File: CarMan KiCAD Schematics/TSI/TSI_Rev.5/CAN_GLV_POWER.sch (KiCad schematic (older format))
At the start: 35 parts, among them K2 G5LE-1-E, K3 SFS2-DC24V, K4 SFS2-DC24V, Q11 TN2130K1-G, U14 Bottom Left, U15 Top Left, U17 Top Right, U2 Bottom Right, U24 TLP293, U41 PDQ10-Q24-D5-D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

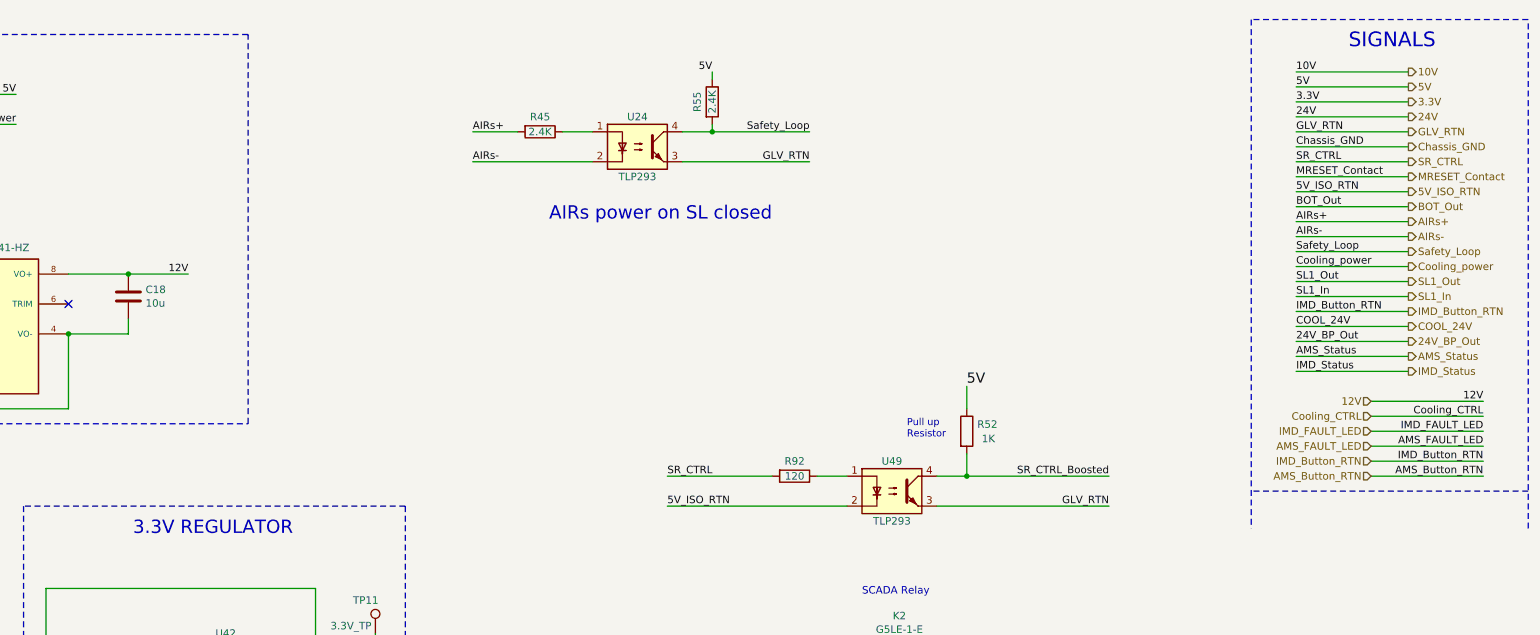
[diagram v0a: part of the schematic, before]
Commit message: Updated Signals and Trace Width
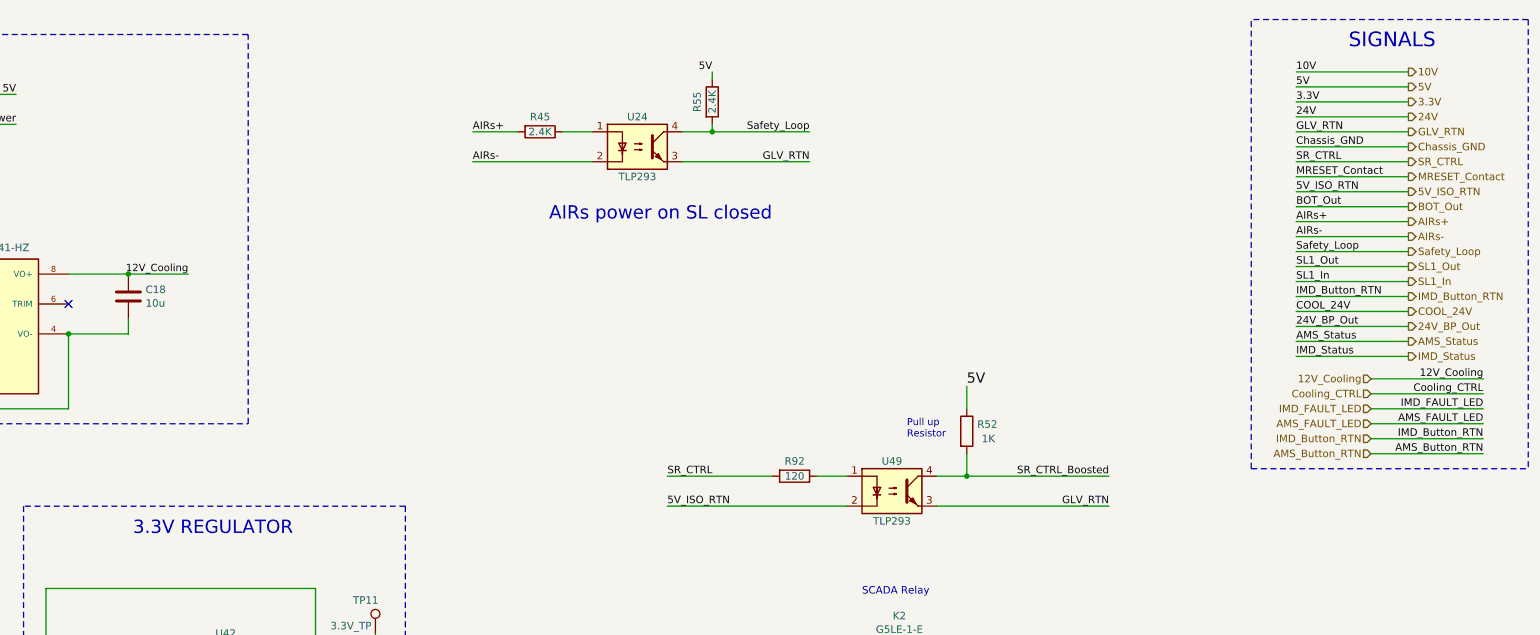
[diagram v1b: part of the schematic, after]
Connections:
- net labels added: 12V_Cooling
- net labels removed: 12V
- wire segments 175 -> 174
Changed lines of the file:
@@
 $Descr A3 16535 11693
 encoding utf-8
-Sheet 6 6
+Sheet 4 6
 Title ""
 Date ""
@@
 Zacky Bear Doesn't Like
 Text Label 7050 2250 2    49   ~ 0
-12V
+12V_Cooling
 Text Notes 10950 1900 2    89   ~ 0
 AIRs power on SL closed
@@
 Text HLabel 15200 1500 2    50   Output ~ 0
 SR_CTRL
-Text Label 14450 2400 0    50   ~ 0
+Text Label 14450 2300 0    50   ~ 0
 SL1_In
-Text HLabel 15200 2400 2    50   Output ~ 0
+Text HLabel 15200 2300 2    50   Output ~ 0
 SL1_In
-Text Label 14450 2300 0    50   ~ 0
+Text Label 14450 2200 0    50   ~ 0
 SL1_Out
-Text HLabel 15200 2300 2    50   Output ~ 0
+Text HLabel 15200 2200 2    50   Output ~ 0
 SL1_Out
-Text Label 14450 2200 0    50   ~ 0
-Cooling_power
-Text HLabel 15200 2200 2    50   Output ~ 0
-Cooling_power
-Text Label 14450 2900 0    50   ~ 0
+Text Label 14450 2800 0    50   ~ 0
 IMD_Status
 Text Label 14450 2100 0    50   ~ 0
 Safety_Loop
-Text HLabel 15200 2900 2    50   Output ~ 0
+Text HLabel 15200 2800 2    50   Output ~ 0
 IMD_Status
 Text HLabel 15200 2100 2    50   Output ~ 0
@@
 Text Notes 4650 8850 0    68   ~ 0
 Dashboard\n
-Text HLabel 15200 2800 2    50   Output ~ 0
+Text HLabel 15200 2700 2    50   Output ~ 0
 AMS_Status
-Text Label 14450 2800 0    50   ~ 0
+Text Label 14450 2700 0    50   ~ 0
 AMS_Status
+Text Label 14450 2400 0    50   ~ 0
+IMD_Button_RTN
+Text HLabel 15200 2400 2    50   Output ~ 0
+IMD_Button_RTN
 Text Label 14450 2500 0    50   ~ 0
-IMD_Button_RTN
+COOL_24V
 Text HLabel 15200 2500 2    50   Output ~ 0
-IMD_Button_RTN
-Text Label 14450 2600 0    50   ~ 0
 COOL_24V
-Text HLabel 15200 2600 2    50   Output ~ 0
-COOL_24V
 Wire Wire Line
 	14450 1600 15200 1600
 Wire Wire Line
+	14450 2300 15200 2300
+Wire Wire Line
+	14450 2700 15200 2700
+Wire Wire Line
+	14450 2500 15200 2500
+Wire Wire Line
 	14450 2400 15200 2400
 Wire Wire Line
-	14450 2800 15200 2800
-Wire Wire Line
-	14450 2600 15200 2600
-Wire Wire Line
-	14450 2500 15200 2500
-Wire Wire Line
 	14450 2200 15200 2200
-Wire Wire Line
-	14450 2300 15200 2300
-Text Label 15700 3100 2    50   ~ 0
-12V
+Text Label 15700 2950 2    50   ~ 0
+12V_Cooling
 Text Label 9600 8200 2    50   ~ 0
 GLV_RTN
@@
 Text Label 6700 9200 0    50   ~ 0
 24V
-Text HLabel 15200 2700 2    50   Output ~ 0
+Text HLabel 15200 2600 2    50   Output ~ 0
 24V_BP_Out
 Wire Wire Line
-	14450 2700 15200 2700
-Text Label 14450 2700 0    50   ~ 0
+	14450 2600 15200 2600
+Text Label 14450 2600 0    50   ~ 0
 24V_BP_Out
 Text Label 10350 9700 2    50   ~ 0
@@
 	14450 2100 15200 2100
 Wire Wire Line
-	14450 2900 15200 2900
-Wire Notes Line
-	16000 3700 14150 3700
-Wire Notes Line
-	16000 3950 16000 550
-Wire Notes Line
-	14150 550  14150 3950
-Wire Wire Line
-	14950 3100 15700 3100
-Wire Wire Line
-	14950 3200 15700 3200
-Wire Wire Line
-	14950 3300 15700 3300
-Wire Wire Line
-	14950 3400 15700 3400
-Wire Wire Line
-	14950 3500 15700 3500
-Wire Wire Line
-	14950 3600 15700 3600
-Text Label 15700 3400 2    50   ~ 0
+	14450 2800 15200 2800
+Wire Wire Line
+	14950 2950 15700 2950
+Wire Wire Line
+	14950 3050 15700 3050
+Wire Wire Line
+	14950 3150 15700 3150
+Wire Wire Line
+	14950 3250 15700 3250
+Wire Wire Line
+	14950 3350 15700 3350
+Wire Wire Line
+	14950 3450 15700 3450
+Text Label 15700 3250 2    50   ~ 0
 AMS_FAULT_LED
-Text HLabel 14950 3400 0    50   Input ~ 0
+Text HLabel 14950 3250 0    50   Input ~ 0
 AMS_FAULT_LED
-Text Label 15700 3600 2    50   ~ 0
+Text Label 15700 3450 2    50   ~ 0
 AMS_Button_RTN
-Text HLabel 14950 3600 0    50   Input ~ 0
+Text HLabel 14950 3450 0    50   Input ~ 0
 AMS_Button_RTN
-Text Label 15700 3500 2    50   ~ 0
+Text Label 15700 3350 2    50   ~ 0
 IMD_Button_RTN
-Text HLabel 14950 3500 0    50   Input ~ 0
+Text HLabel 14950 3350 0    50   Input ~ 0
 IMD_Button_RTN
-Text Label 15700 3200 2    50   ~ 0
+Text Label 15700 3050 2    50   ~ 0
 Cooling_CTRL
-Text HLabel 14950 3200 0    50   Input ~ 0
+Text HLabel 14950 3050 0    50   Input ~ 0
 Cooling_CTRL
-Text HLabel 14950 3100 0    50   Input ~ 0
-12V
-Text Label 15700 3300 2    50   ~ 0
+Text HLabel 14950 2950 0    50   Input ~ 0
+12V_Cooling
+Text Label 15700 3150 2    50   ~ 0
 IMD_FAULT_LED
-Text HLabel 14950 3300 0    50   Input ~ 0
+Text HLabel 14950 3150 0    50   Input ~ 0
 IMD_FAULT_LED
 Wire Wire Line
@@
 Wire Notes Line
 	2950 650  2950 3250
+Wire Notes Line
+	16000 550  16000 3550
+Wire Notes Line
+	14150 3550 16000 3550
+Wire Notes Line
+	14150 3550 14150 550
 $EndSCHEMATC

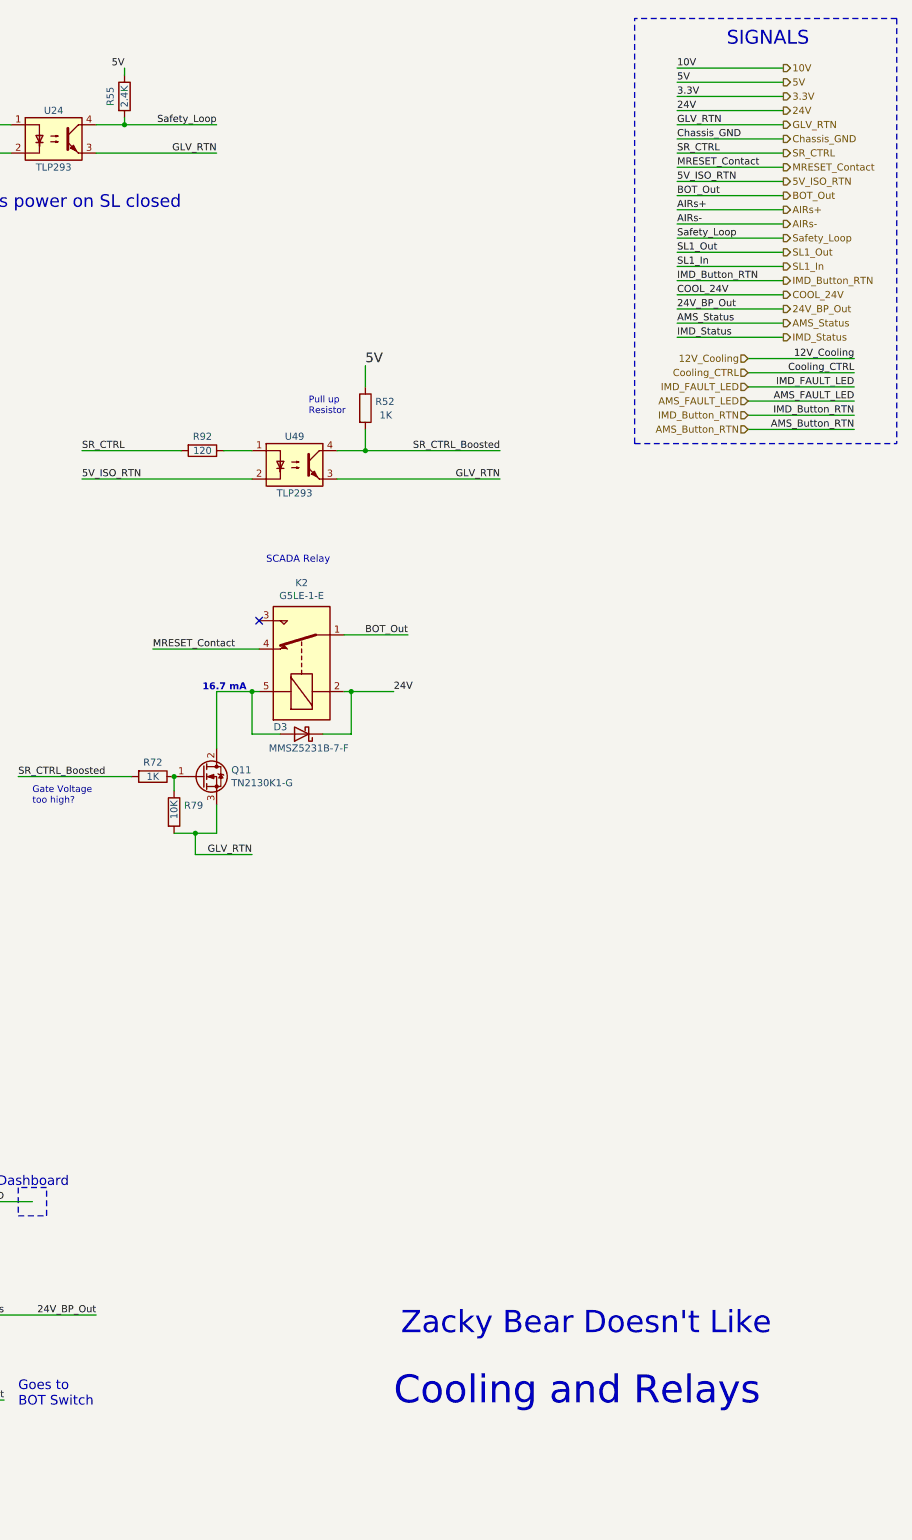
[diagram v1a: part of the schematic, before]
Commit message: Logic Edge Cuts, TSI fixed safety loop and fault signals to dash-added inverters and V dividers, updated pcb and schematic
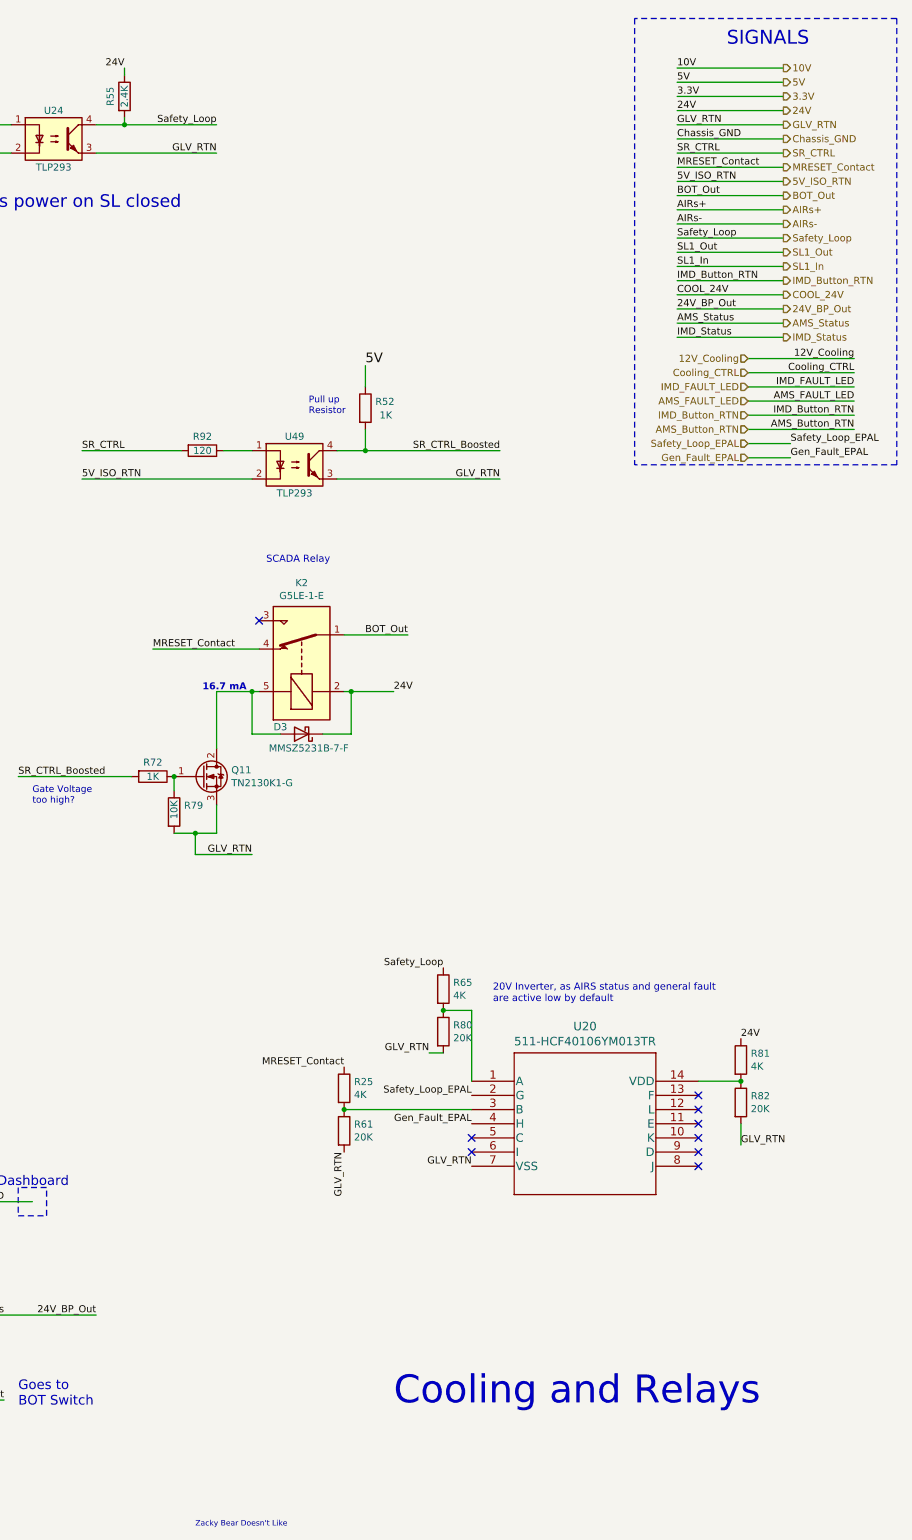
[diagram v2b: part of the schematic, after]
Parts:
- added R25, R65, R81: 4K, Resistor_SMD:R_0805_2012Metric_Pad1.15x1.40mm_HandSolder, symbol Device:R
- added R61, R80, R82: 20K, Resistor_SMD:R_0805_2012Metric_Pad1.15x1.40mm_HandSolder, symbol Device:R
- added U20: 511-HCF40106YM013TR, CarMan General Footprints:511-HCF40106YM013TR, symbol CarMan_KiCAD_Library:511-HCF40106YM013TR
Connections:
- net labels added: Gen_Fault_EPAL, Safety_Loop_EPAL
- wire segments 174 -> 182
- no-connect marks 9 -> 17
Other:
- note added: "20V Inverter, as AIRS status and general fault\nare active low by default"
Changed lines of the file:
@@
 Wire Wire Line
 	11450 5300 11500 5300
-Text Notes 12500 9850 0    157  ~ 0
+Text Notes 11050 11200 0    39   ~ 0
 Zacky Bear Doesn't Like
 Text Label 7050 2250 2    49   ~ 0
@@
 Safety_Loop
 Text Label 10550 900  2    50   ~ 0
-5V
+24V
 Wire Wire Line
 	10350 1300 10550 1300
@@
 Wire Notes Line
 	2950 650  2950 3250
-Wire Notes Line
-	16000 550  16000 3550
-Wire Notes Line
-	14150 3550 16000 3550
-Wire Notes Line
-	14150 3550 14150 550
+$Comp
+L CarMan_KiCAD_Library:511-HCF40106YM013TR U20
+U 1 1 60107413
+P 13000 8050
+F 0 "U20" H 13800 8437 60  0000 C CNN
+F 1 "511-HCF40106YM013TR" H 13800 8331 60  0000 C CNN
+F 2 "CarMan General Footprints:511-HCF40106YM013TR" H 13800 8290 60  0001 C CNN
+F 3 "https://www.mouser.com/datasheet/2/389/hcf40106-954733.pdf" H 13800 8331 60  0001 C CNN
+	1    13000 8050
+	1    0    0    -1
+$EndComp
+$Comp
+L Device:R R81
+U 1 1 60112B09
+P 14900 7900
+F 0 "R81" H 14970 7946 50  0000 L CNN
+F 1 "4K" H 14970 7855 50  0000 L CNN
+F 2 "Resistor_SMD:R_0805_2012Metric_Pad1.15x1.40mm_HandSolder" V 14830 7900 50  0001 C CNN
+F 3 "~" H 14900 7900 50  0001 C CNN
+	1    14900 7900
+	1    0    0    -1
+$EndComp
+$Comp
+L Device:R R82
+U 1 1 60113131
+P 14900 8200
+F 0 "R82" H 14970 8246 50  0000 L CNN
+F 1 "20K" H 14970 8155 50  0000 L CNN
+F 2 "Resistor_SMD:R_0805_2012Metric_Pad1.15x1.40mm_HandSolder" V 14830 8200 50  0001 C CNN
+F 3 "~" H 14900 8200 50  0001 C CNN
+	1    14900 8200
+	1    0    0    -1
+$EndComp
+Text Label 14900 7750 0    50   ~ 0
+24V
+Text Label 14900 8500 0    50   ~ 0
+GLV_RTN
+Wire Wire Line
+	14900 8350 14900 8500
+Wire Wire Line
+	14600 8050 14900 8050
+Connection ~ 14900 8050
+Text Label 13000 8650 2    50   ~ 0
+GLV_RTN
+Text Label 12800 7250 2    50   ~ 0
+Safety_Loop
+Text Label 12100 7950 2    50   ~ 0
+MRESET_Contact
+Text HLabel 14950 3550 0    50   Input ~ 0
+Safety_Loop_EPAL
+Text HLabel 14950 3650 0    50   Input ~ 0
+Gen_Fault_EPAL
+Text Label 15250 3550 0    50   ~ 0
+Safety_Loop_EPAL
+Text Label 15250 3650 0    50   ~ 0
+Gen_Fault_EPAL
+Wire Wire Line
+	14950 3550 15250 3550
+Wire Wire Line
+	14950 3650 15250 3650
+Text Label 13000 8350 2    50   ~ 0
+Gen_Fault_EPAL
+Text Label 13000 8150 2    50   ~ 0
+Safety_Loop_EPAL
+NoConn ~ 13000 8450
+NoConn ~ 13000 8550
+NoConn ~ 14600 8650
+NoConn ~ 14600 8550
+NoConn ~ 14600 8450
+NoConn ~ 14600 8350
+NoConn ~ 14600 8250
+NoConn ~ 14600 8150
+$Comp
+L Device:R R65
+U 1 1 601AB819
+P 12800 7400
+F 0 "R65" H 12870 7446 50  0000 L CNN
+F 1 "4K" H 12870 7355 50  0000 L CNN
+F 2 "Resistor_SMD:R_0805_2012Metric_Pad1.15x1.40mm_HandSolder" V 12730 7400 50  0001 C CNN
+F 3 "~" H 12800 7400 50  0001 C CNN
+	1    12800 7400
+	1    0    0    -1
+$EndComp
+$Comp
+L Device:R R80
+U 1 1 601AB823
+P 12800 7700
+F 0 "R80" H 12870 7746 50  0000 L CNN
+F 1 "20K" H 12870 7655 50  0000 L CNN
+F 2 "Resistor_SMD:R_0805_2012Metric_Pad1.15x1.40mm_HandSolder" V 12730 7700 50  0001 C CNN
+F 3 "~" H 12800 7700 50  0001 C CNN
+	1    12800 7700
+	1    0    0    -1
+$EndComp
+$Comp
+L Device:R R25
+U 1 1 601C082D
+P 12100 8100
+F 0 "R25" H 12170 8146 50  0000 L CNN
+F 1 "4K" H 12170 8055 50  0000 L CNN
+F 2 "Resistor_SMD:R_0805_2012Metric_Pad1.15x1.40mm_HandSolder" V 12030 8100 50  0001 C CNN
+F 3 "~" H 12100 8100 50  0001 C CNN
+	1    12100 8100
+	1    0    0    -1
+$EndComp
+$Comp
+L Device:R R61
+U 1 1 601C0837
+P 12100 8400
+F 0 "R61" H 12170 8446 50  0000 L CNN
+F 1 "20K" H 12170 8355 50  0000 L CNN
+F 2 "Resistor_SMD:R_0805_2012Metric_Pad1.15x1.40mm_HandSolder" V 12030 8400 50  0001 C CNN
+F 3 "~" H 12100 8400 50  0001 C CNN
+	1    12100 8400
+	1    0    0    -1
+$EndComp
+Text Label 12100 8550 3    50   ~ 0
+GLV_RTN
+Text Label 12700 7850 2    50   ~ 0
+GLV_RTN
+Wire Wire Line
+	12800 7850 12700 7850
+Wire Wire Line
+	12800 7550 13000 7550
+Wire Wire Line
+	13000 7550 13000 8050
+Connection ~ 12800 7550
+Wire Wire Line
+	12100 8250 13000 8250
+Connection ~ 12100 8250
+Text Notes 13150 7500 0    50   ~ 0
+20V Inverter, as AIRS status and general fault\nare active low by default
+Wire Notes Line
+	16000 3700 14150 3700
+Wire Notes Line
+	16000 550  16000 3700
+Wire Notes Line
+	14150 550  14150 3700
 $EndSCHEMATC
